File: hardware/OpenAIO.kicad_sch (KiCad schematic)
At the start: 16 parts, among them U24 AIO_outline, U25 INA186A3IDCKR

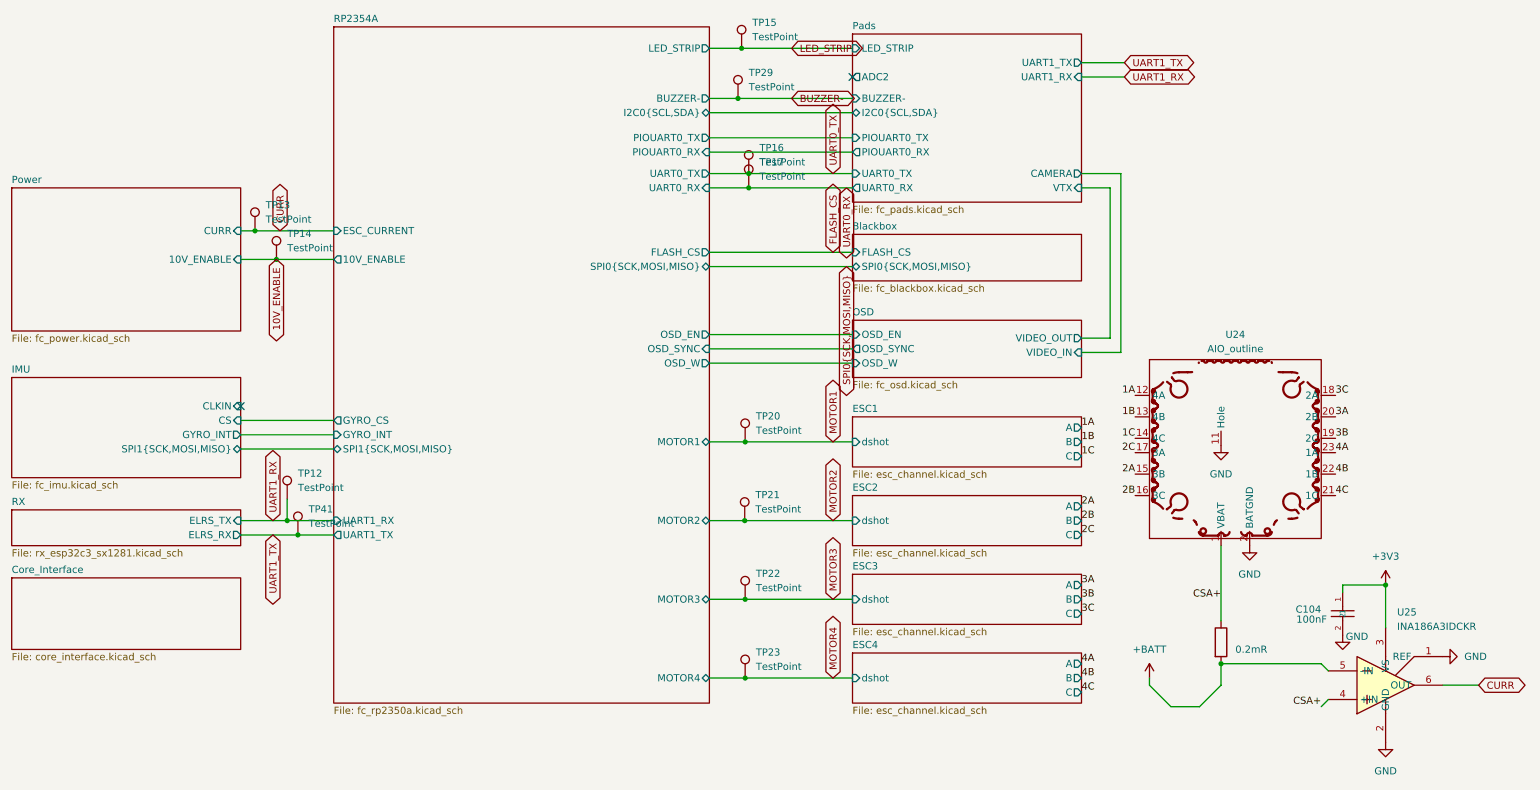
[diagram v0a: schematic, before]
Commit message: One board: the flight controller is the OpenFC-Core module
The core sheets, the second board project and the multiboard split are
gone; OpenDrone-Core sits on the root schematic as J1 and its land is on
the board at (78.0, 61.65) with the existing routing kept. Board settings
and 2 oz rules carried over from the Base project. Docs updated.

Co-Authored-By: Claude Fable 5 <noreply@anthropic.com>
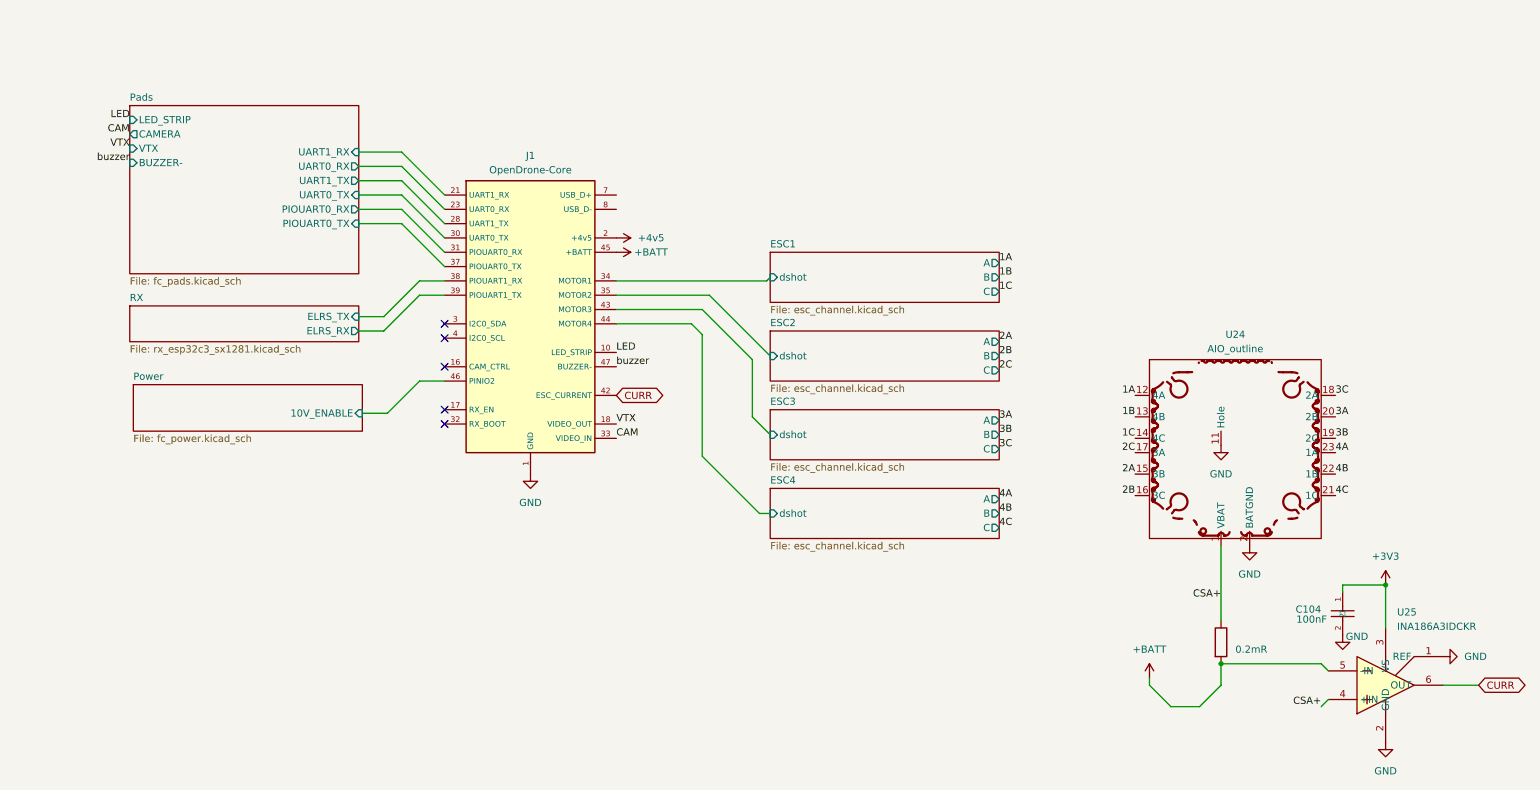
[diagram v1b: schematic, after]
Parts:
- removed TP12, TP13, TP14, TP15, TP16, TP17, TP20, TP21, TP22, TP23, TP29, TP41: TestPoint, TestPoint:TestPoint_Pad_D1.0mm, symbol Connector:TestPoint
- added J1: OpenDrone-Core, lib:OpenDrone-Core_LGA_land, symbol lib:OpenDrone-Core
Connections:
- net +BATT: now also J1.45 (+BATT)
- net CURR: now also J1.42 (ESC_CURRENT)
- net GND: now also J1.1 (GND), J1.11 (GND), J1.12 (GND), J1.13 (GND), J1.14 (GND), J1.15 (GND), J1.19 (GND), J1.20 (GND), J1.22 (GND), J1.24 (GND), J1.25 (GND), J1.26 (GND), J1.27 (GND), J1.29 (GND), J1.36 (GND), J1.40 (GND), J1.41 (GND), J1.48 (GND), J1.49 (GND), J1.5 (GND), J1.50 (GND), J1.51 (GND), J1.52 (GND), J1.53 (GND), J1.54 (GND), J1.6 (GND), J1.9 (GND)
- net Pads/PIOUART0_RX: now also J1.31 (PIOUART0_RX)
- net Pads/PIOUART0_TX: now also J1.37 (PIOUART0_TX)
- new net +4v5: J1.2 (+4v5)
- new net CAM: J1.33 (VIDEO_IN)
- new net ESC1/dshot: J1.34 (MOTOR1)
- new net ESC2/dshot: J1.35 (MOTOR2)
- new net ESC3/dshot: J1.43 (MOTOR3)
- new net ESC4/dshot: J1.44 (MOTOR4)
- new net LED: J1.10 (LED_STRIP)
- new net Pads/UART0_RX: J1.23 (UART0_RX)
- new net Pads/UART0_TX: J1.30 (UART0_TX)
- new net Pads/UART1_RX: J1.21 (UART1_RX)
- new net Pads/UART1_TX: J1.28 (UART1_TX)
- new net Power/10V_ENABLE: J1.46 (PINIO2)
- new net RX/ELRS_RX: J1.39 (PIOUART1_TX)
- new net RX/ELRS_TX: J1.38 (PIOUART1_RX)
- new net VTX: J1.18 (VIDEO_OUT)
- new net buzzer: J1.47 (BUZZER-)
- no-connect marks 2 -> 5
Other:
- removed sheet Blackbox
- removed sheet Core_Interface
- removed sheet IMU
- removed sheet OSD
- removed sheet RP2354A
- sheet Pads ports: added none; removed ADC2, I2C0{SCL,SDA}
- sheet Power ports: added none; removed CURR
